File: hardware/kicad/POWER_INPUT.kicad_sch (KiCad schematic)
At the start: 0 parts

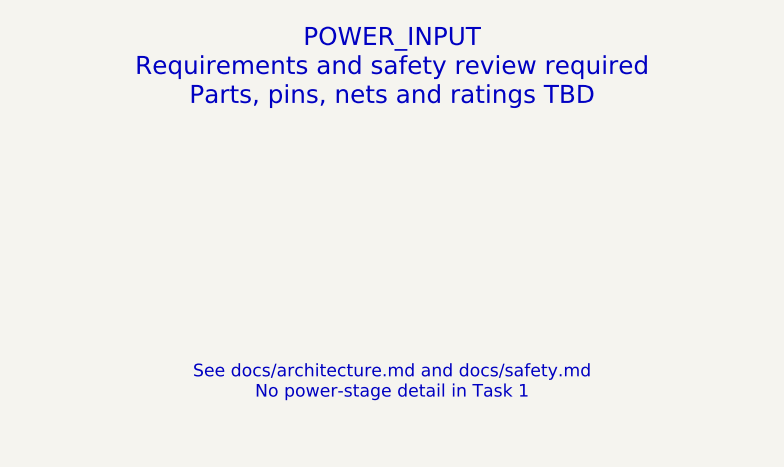
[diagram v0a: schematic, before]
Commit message: hardware: update existing KiCad architecture and add precharge sheet
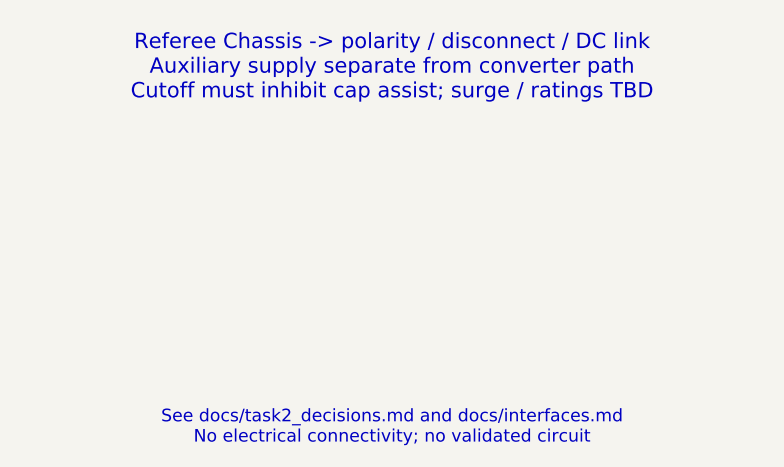
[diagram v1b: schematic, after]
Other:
- note added: "Referee Chassis -> polarity / disconnect / DC link Auxiliary supply separate from converter path Cutoff must inhibit cap assist; surge / ratings TBD"
- note added: "See docs/task2_decisions.md and docs/interfaces.md No electrical connectivity; no validated circuit"
- note removed: "POWER_INPUT Requirements and safety review required Parts, pins, nets and ratings TBD"
- note removed: "See docs/architecture.md and docs/safety.md No power-stage detail in Task 1"
- title: POWER_INPUT - Placeholder -> POWER_INPUT - Task 2 Proposal

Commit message: hardware: implement prototype Rev A electrical schematic
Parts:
- added D1: SMBJ28A / no surge-energy guarantee, Diode_SMD:D_SMB, symbol RevA:D
- added D2: SS110 flyback candidate / release delay MUST VERI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, Diode_SMD:D_SMA, symbol RevA:D
- added F1: ATOF 58V 10A candidate / I2t & breaking coordinat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, symbol RevA:FUSE
- added J1: ROBOT BUS terminal / keyed DC-rated connector TBD, symbol RevA:J2
- added J2: BUS_ISO external actuator+feedback, symbol RevA:J4
- added J3: referee permit interface / no bypass, symbol RevA:J3
- added J4: external BUS-derived actuator 12V supply / budget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, symbol RevA:J2
- added K1: BUS_ISO external NO contact / AEV14012 candidate, symbol RevA:CONTACT
- added Q1: CSD18540Q5B, Package_SON:VSONP-8-1EP_5x6_P1.27mm, symbol RevA:CSD18540Q5B
- added Q2: BC857B, Package_TO_SOT_SMD:SOT-23, symbol RevA:Q_PNP
- added Q3: BC847B, Package_TO_SOT_SMD:SOT-23, symbol RevA:Q_NPN
- added R1, R2, R3, R7, R8: 10k, Resistor_SMD:R_0805_2012Metric, symbol RevA:R
- added R4: 4.7k, Resistor_SMD:R_0805_2012Metric, symbol RevA:R
- added R5: 100k, Resistor_SMD:R_0805_2012Metric, symbol RevA:R
- added R6: 47R, Resistor_SMD:R_0805_2012Metric, symbol RevA:R
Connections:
- new net ACTUATOR_12V: D2.1 (K), J2.1 (P1), J4.1 (P1), K1.3 (COIL_P), Q2.2 (E), R2.2 (B)
- new net BUS_FUSED: D1.1 (K), F1.2 (B), K1.1 (COM)
- new net BUS_ISOLATED: K1.2 (NO)
- new net BUS_ISO_COIL_GATE: Q1.2 (G_DS4), R1.1 (A), R6.2 (B)
- new net BUS_ISO_COIL_M: D2.2 (A), J2.2 (P2), K1.4 (COIL_M), Q1.3 (D_DS5_6_7_8)
- new net BUS_ISO_DRIVE: R4.1 (A)
- new net BUS_ISO_FB: J2.3 (P3), R7.1 (A)
- new net BUS_ISO_NPN_C: Q3.3 (C), R3.2 (B)
- new net BUS_ISO_NPN_C_BASE: Q3.1 (B), R4.2 (B), R5.1 (A)
- new net BUS_ISO_PNP_B: Q2.1 (B), R2.1 (A), R3.1 (A)
- new net BUS_ISO_PNP_C: Q2.3 (C), R6.1 (A)
- new net BUS_RAW: F1.1 (A), J1.1 (P1), J3.1 (P1)
- new net GND: D1.2 (A), J1.2 (P2), J2.4 (P4), J3.2 (P2), J4.2 (P2), Q1.1 (S_DS1_2_3), Q3.2 (E), R1.2 (B), R5.2 (B), R8.2 (B)
- new net REFEREE_PERMIT: J3.3 (P3), R8.1 (A)
- new net V3V3: R7.2 (B)
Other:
- note added: "Aux input is BUS_FUSED upstream of NO isolate. No bank-fed control rail."
- note added: "External NO contacts need independent DC interrupt review; AEV14012 is oversized candidate, not released BOM."
- note added: "Fuse+TVS values provisional. TVS cathode positive; reverse insertion is not authorized."
- note removed: "Referee Chassis -> polarity / disconnect / DC link Auxiliary supply separate from converter path Cutoff must inhibit cap assist; surge / ratings TBD"
- note removed: "See docs/task2_decisions.md and docs/interfaces.md No electrical connectivity; no validated circuit"
- title: POWER_INPUT - Task 2 Proposal -> POWER_INPUT / Prototype Rev A draft

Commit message: hardware: refine Rev A protection and passive selections
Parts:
- removed J4: external BUS-derived actuator 12V supply / budget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, symbol RevA:J2
- added F2: 0997005.WXN / MINI997 58V5A / external 0FHM0002ZX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, symbol RevA:FUSE
- added U1: Blue Sea6006 / external manual source disconnect;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, symbol RevA:DISCONNECT
- added U2: DDR-60L-12 / external bench actuator supply, symbol RevA:DDR60L12
- D1: MPN (none) -> SMBJ28A
- D2: value SS110 flyback candidate / release delay MUST VERIFY -> SMBJ18CA bidirectional coil suppression / release MUST VERIFY; footprint Diode_SMD:D_SMA -> Diode_SMD:D_SMB; MPN (none) -> SMBJ18CA
- F1: value ATOF 58V 10A candidate / I2t & breaking coordination TBD -> 0997010.WXN / MINI997 58V10A / external 0FHM0002ZXJM holder; MPN (none) -> 0997010.WXN
- J1: value ROBOT BUS terminal / keyed DC-rated connector TBD -> ROBOT BUS / external covered bolted power terminals
- J2: value BUS_ISO external actuator+feedback -> BUS_ISO actuator+reserved diagnostic / no intrinsic auxiliary contact
- K1: value BUS_ISO external NO contact / AEV14012 candidate -> BUS_ISO external NO contact / AEV14012 bench selection; MPN (none) -> AEV14012
- Q1: MPN (none) -> CSD18540Q5B
- Q2: MPN (none) -> BC857B,215
- Q3: MPN (none) -> BC847B,215
- R1, R2, R3, R7, R8: MPN (none) -> CRCW080510K0FKEA
- R4: MPN (none) -> CRCW08054K70FKEA
- R5: MPN (none) -> CRCW0805100KFKEA
- R6: MPN (none) -> CRCW080547R0FKEA
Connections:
- net V3V3 is gone; now on net GND: R7.2 (B)
- net ACTUATOR_12V: now also U2.3 (VO_P), U2.4 (VO_P)
- net BUS_RAW: now also F2.1 (A), U1.2 (SWITCHED); no longer J1.1 (P1)
- net GND: now also U2.1 (VO_M), U2.2 (VO_M), U2.6 (VIN_M)
- new net ACTUATOR_INPUT: F2.2 (B), U2.5 (VIN_P)
- new net BUS_ROBOT_INPUT: J1.1 (P1), U1.1 (COM)
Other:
- note added: "Four AEV14012 main/bypass contacts, 12V coils; external DDR-60L-12. Bench only: total contact mass about1.6kg."
- note removed: "External NO contacts need independent DC interrupt review; AEV14012 is oversized candidate, not released BOM."
- moved on the sheet: D1, D2, F1, J2, J3, K1, Q1, Q2, Q3, R1, R2, R3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
